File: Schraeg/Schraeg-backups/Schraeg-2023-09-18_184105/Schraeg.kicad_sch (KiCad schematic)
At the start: 29 parts, among them SW1 SW_SP3T, SW2 SW_SP3T, SW3 SW_SP3T, SW4 SW_SP3T

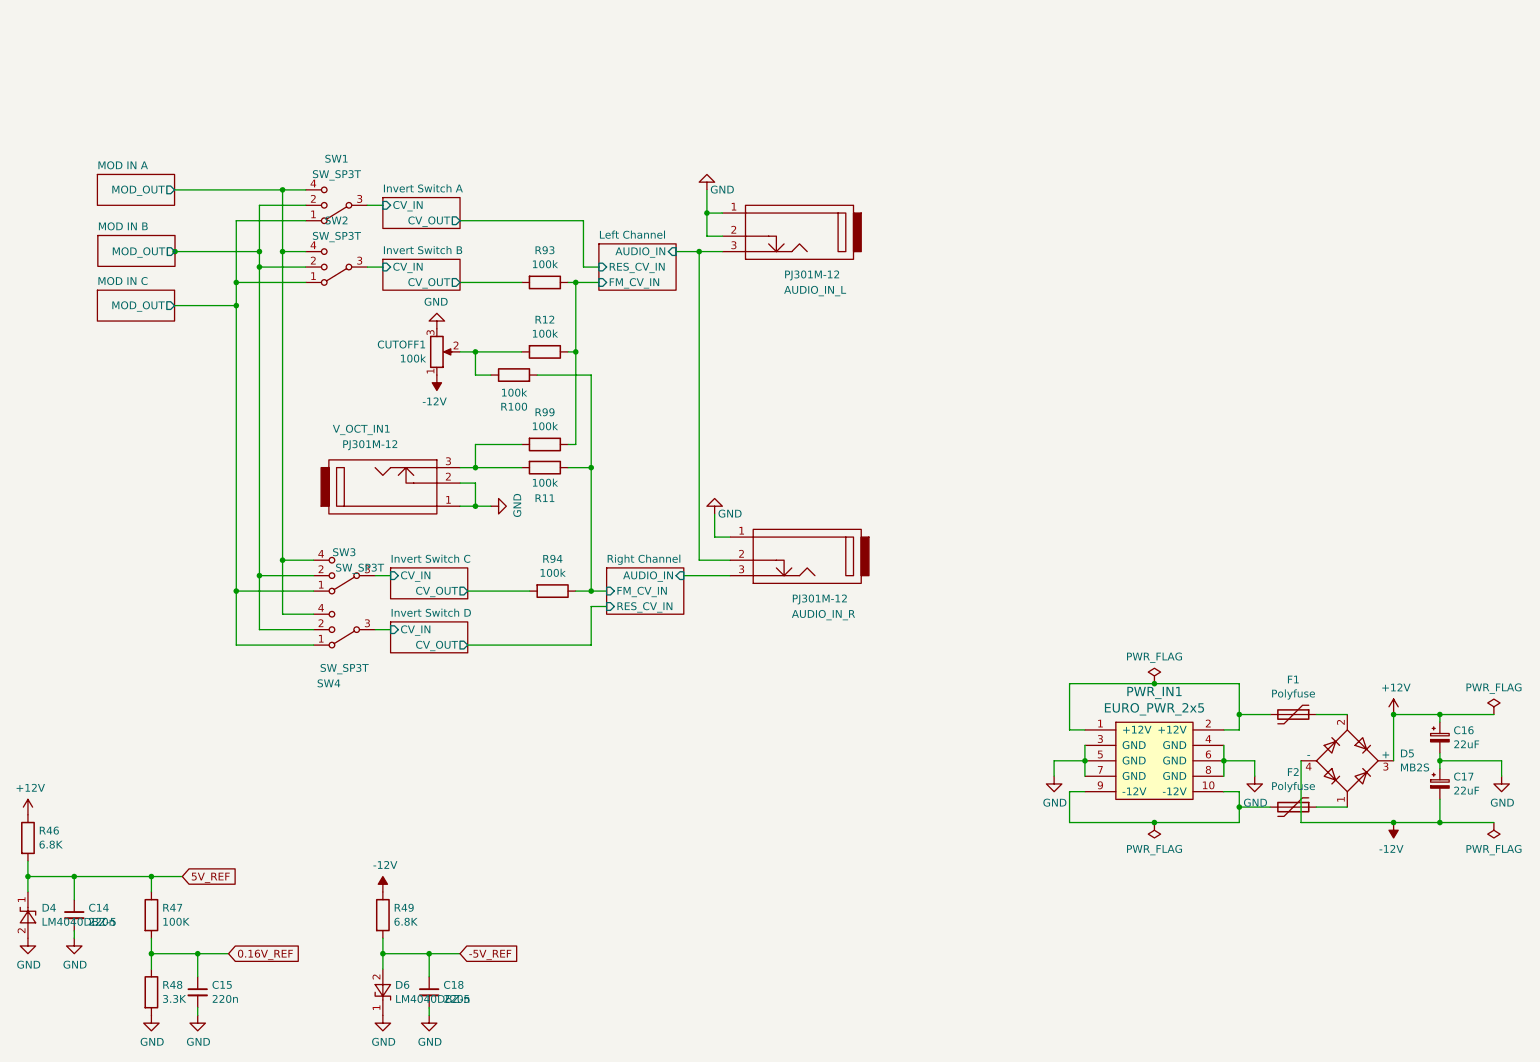
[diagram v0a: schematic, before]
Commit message: fixes filter schematic
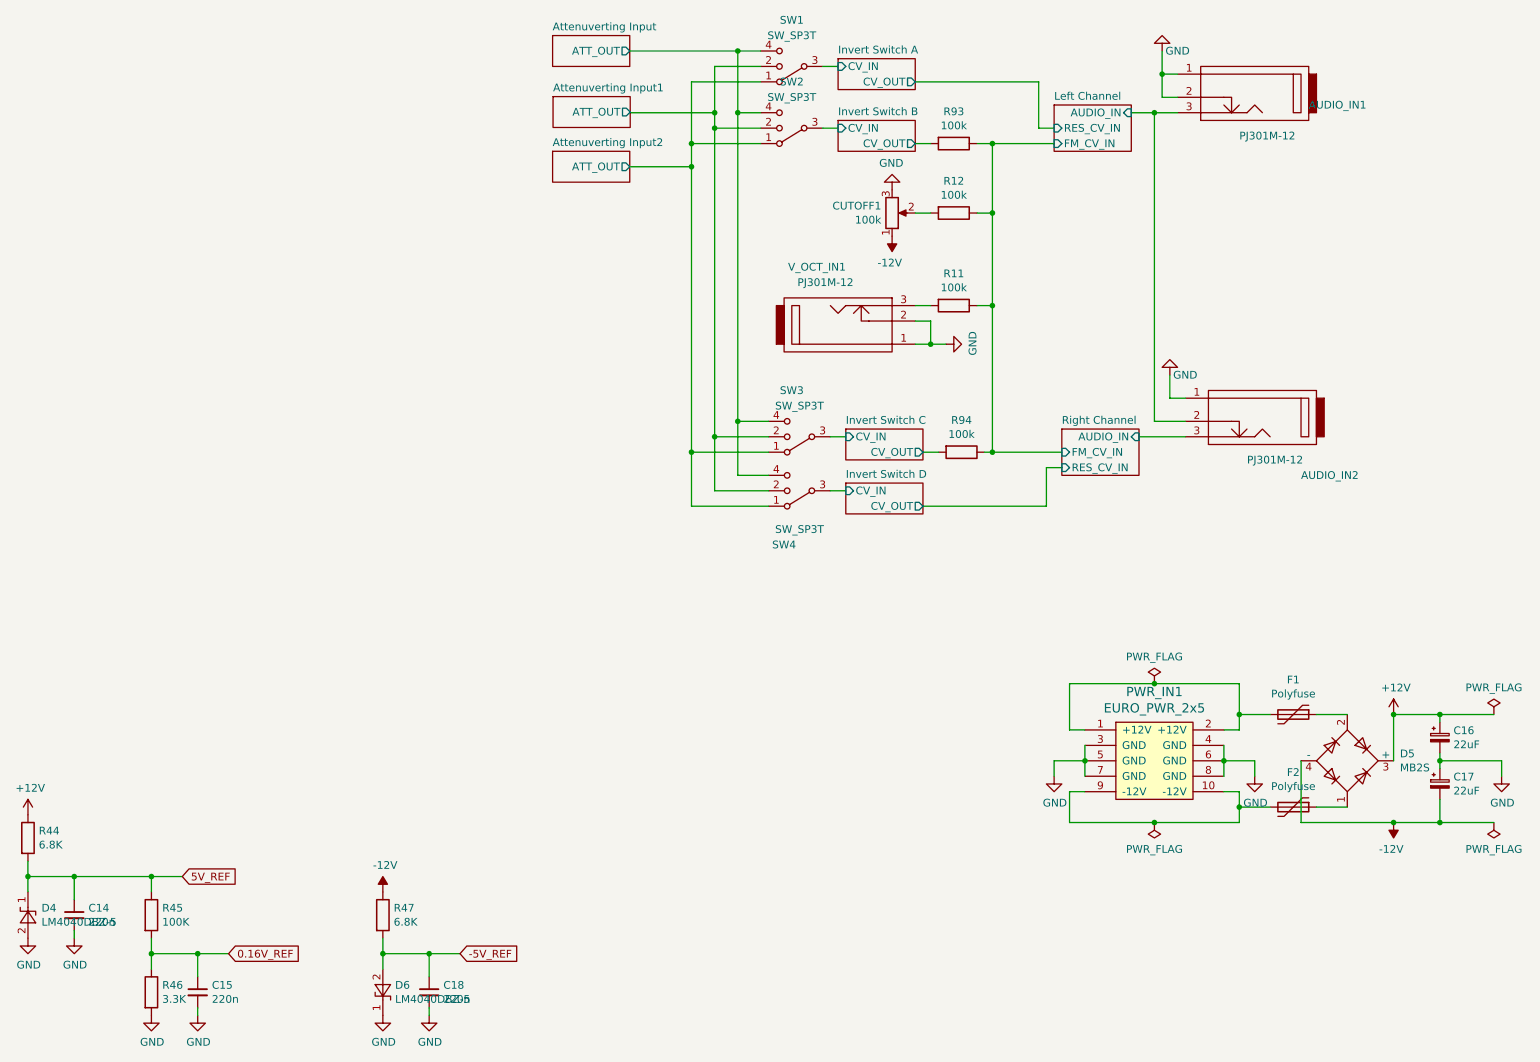
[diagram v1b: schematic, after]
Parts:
- removed R100, R99: 100k, Resistor_SMD:R_0603_1608Metric_Pad1.05x0.95mm_HandSolder, symbol Device:R
- renumbered AUDIO_IN_L to AUDIO_IN1, AUDIO_IN_R to AUDIO_IN2, R46 to R44, R47 to R45, R48 to R46, R49 to R47
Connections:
- net Right Channel/FM_CV_IN is gone; now on net Left Channel/FM_CV_IN: R11.1, R94.1
- net Attenuverting Input/MOD_OUT renamed Attenuverting Input/ATT_OUT
- net Attenuverting Input1/MOD_OUT: no longer names the net of SW1.2, SW2.2, SW3.2, SW4.2
- net Attenuverting Input2/MOD_OUT renamed Attenuverting Input2/ATT_OUT
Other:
- sheet MOD IN A renamed Attenuverting Input
- sheet MOD IN B renamed Attenuverting Input1
- sheet MOD IN C renamed Attenuverting Input2
- sheet Attenuverting Input ports: added ATT_OUT; removed MOD_OUT
- sheet Attenuverting Input1 ports: added ATT_OUT; removed MOD_OUT
- sheet Attenuverting Input2 ports: added ATT_OUT; removed MOD_OUT
- moved on the sheet: AUDIO_IN1, AUDIO_IN2, CUTOFF1, R11, R12, R93, R94, SW1, SW2, SW3, SW4, V_OCT_IN1
